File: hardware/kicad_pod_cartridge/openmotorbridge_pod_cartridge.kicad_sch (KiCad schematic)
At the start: 0 parts

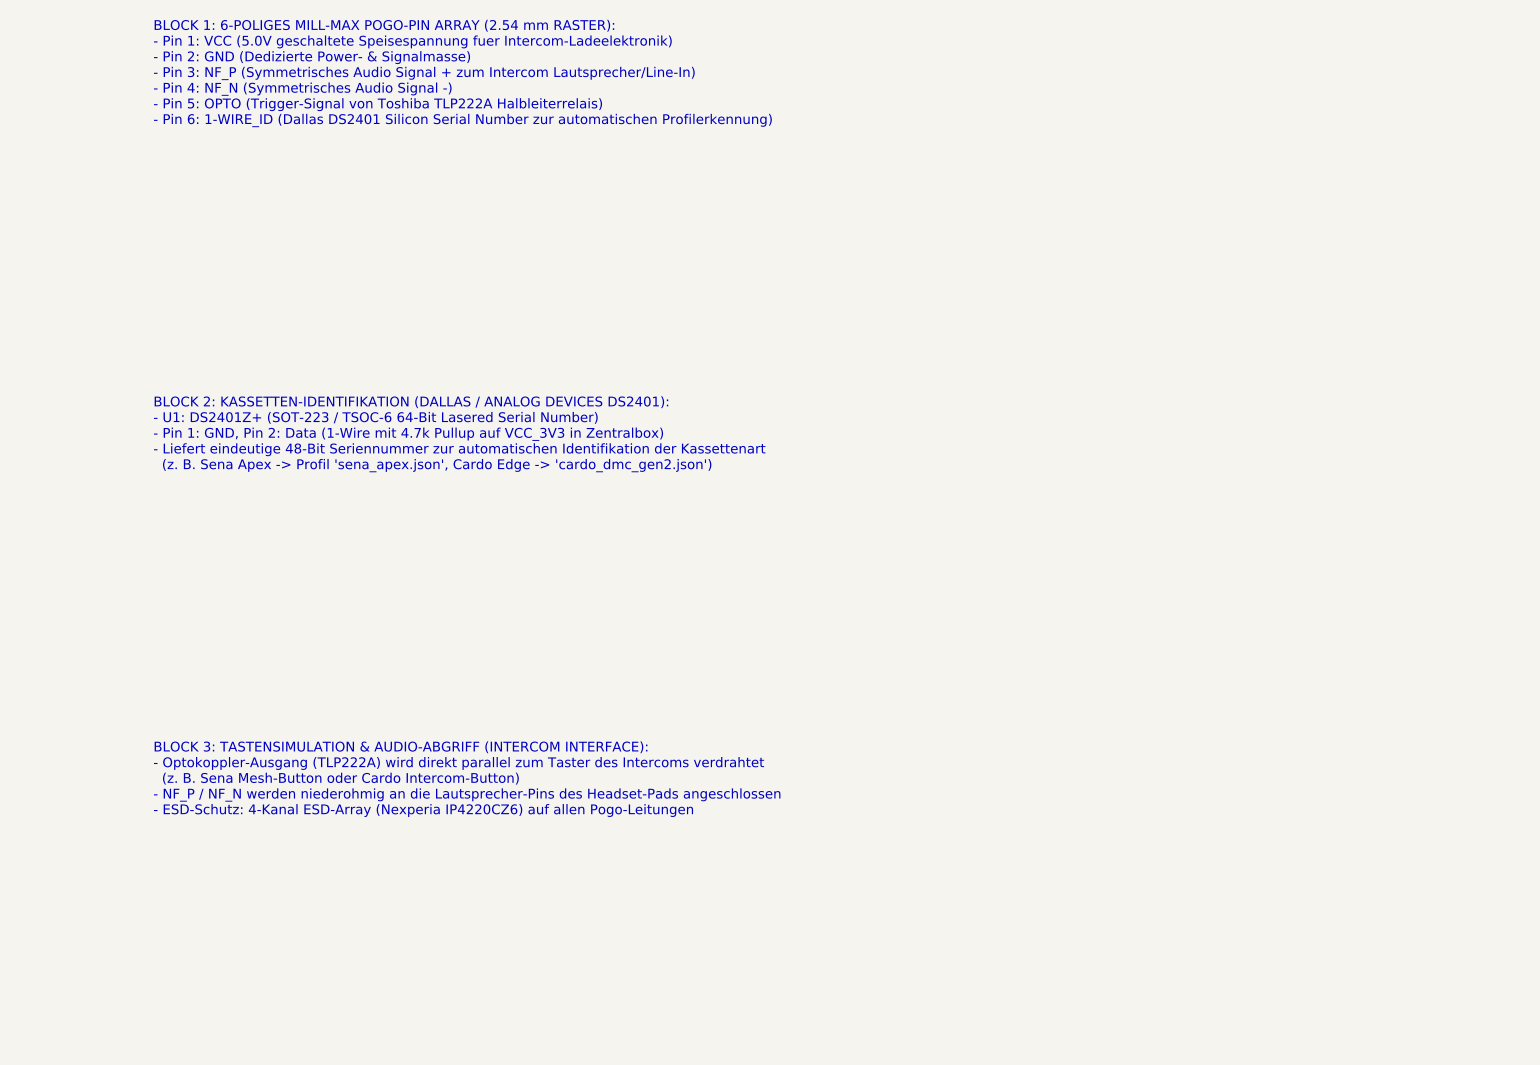
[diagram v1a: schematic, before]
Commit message: fix(kicad): Finalize KiCad 10 Pod 3 Transceiver and Universal Cartridge schematics and verified PDF exports
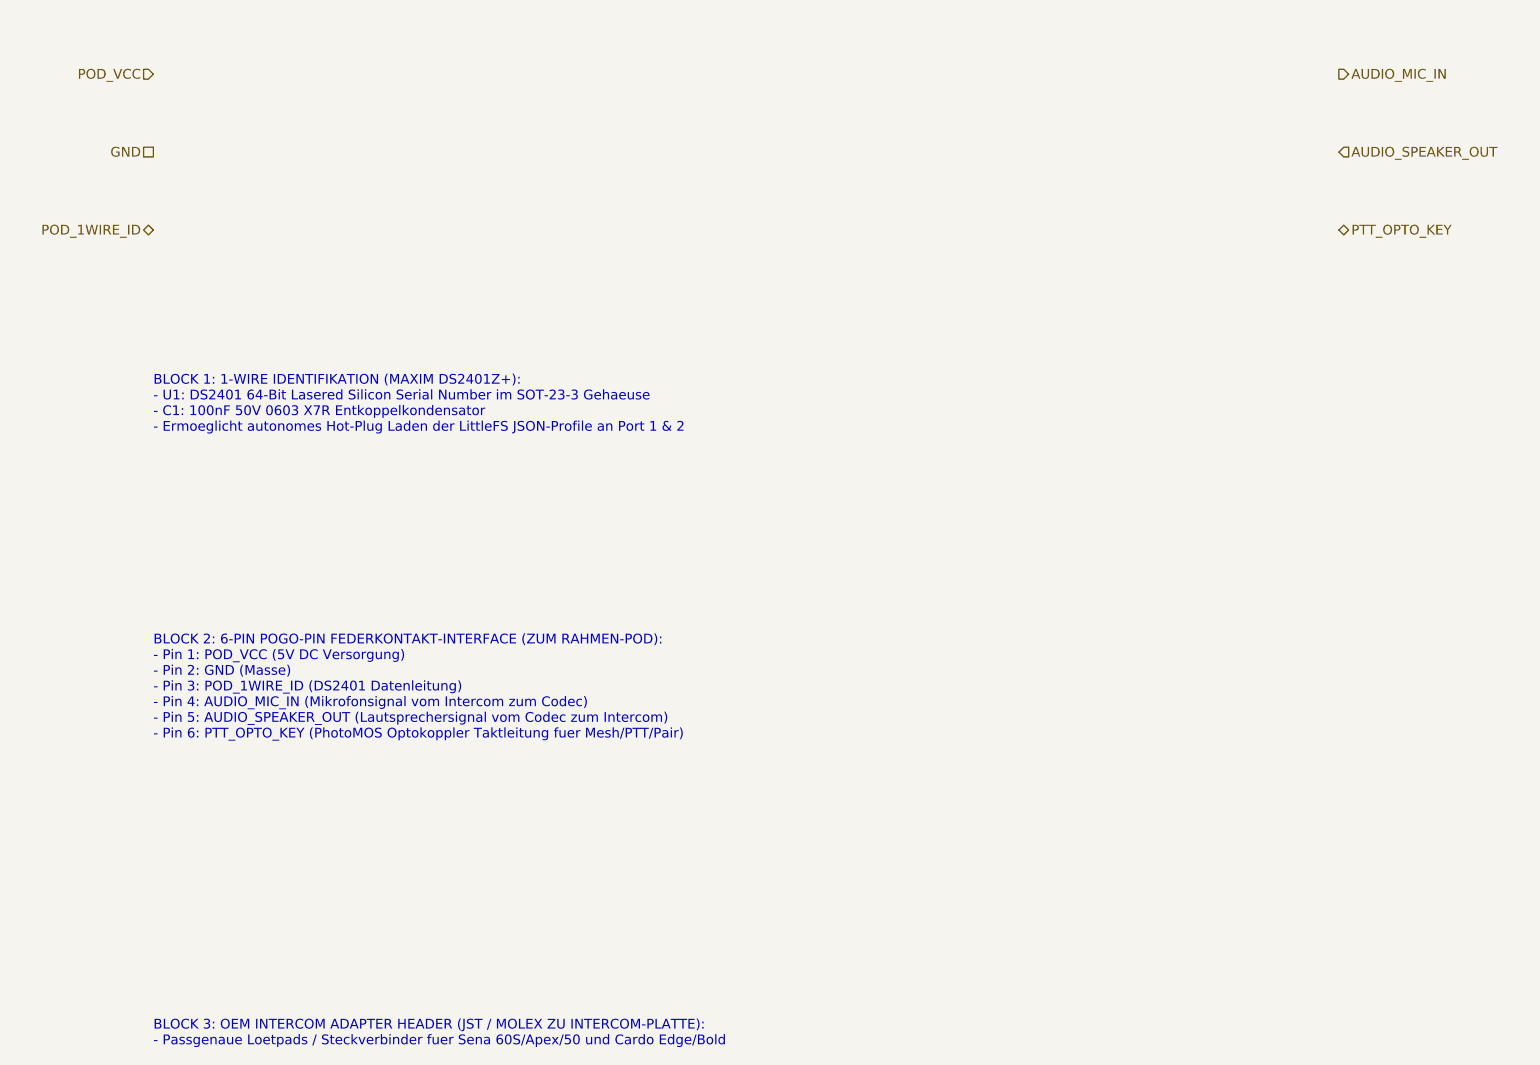
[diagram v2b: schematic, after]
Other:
- note added: "BLOCK 1: 1-WIRE IDENTIFIKATION (MAXIM DS2401Z+): - U1: DS2401 64-Bit Lasered Silicon Serial Number im SOT-23-3 Gehaeuse - C1: 100nF 50V 0603 X7R Entkoppelkondensator - Ermoeglicht autonomes Hot-Plug Laden der LittleFS JSON-Profile an Port 1 & 2"
- note added: "BLOCK 2: 6-PIN POGO-PIN FEDERKONTAKT-INTERFACE (ZUM RAHMEN-POD): - Pin 1: POD_VCC (5V DC Versorgung) - Pin 2: GND (Masse) - Pin 3: POD_1WIRE_ID (DS2401 Datenleitung) - Pin 4: AUDIO_MIC_IN (Mikrofonsignal vom Intercom zum Codec) - Pin 5: AUDIO_SPEAKER_OUT (Lautsprechersignal vom Codec zum Intercom) - Pin 6: PTT_OPTO_KEY (PhotoMOS Optokoppler Taktleitung fuer Mesh/PTT/Pair)"
- note added: "BLOCK 3: OEM INTERCOM ADAPTER HEADER (JST / MOLEX ZU INTERCOM-PLATTE): - Passgenaue Loetpads / Steckverbinder fuer Sena 60S/Apex/50 und Cardo Edge/Bold"
- note removed: "BLOCK 1: 6-POLIGES MILL-MAX POGO-PIN ARRAY (2.54 mm RASTER): - Pin 1: VCC (5.0V geschaltete Speisespannung fuer Intercom-Ladeelektronik) - Pin 2: GND (Dedizierte Power- & Signalmasse) - Pin 3: NF_P (Symmetrisches Audio Signal + zum Intercom Lautsprecher/Line-In) - Pin 4: NF_N (Symmetrisches Audio Signal -) - Pin 5: OPTO (Trigger-Signal von Toshiba TLP222A Halbleiterrelais) - Pin 6: 1-WIRE_ID (Dal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"
- note removed: "BLOCK 2: KASSETTEN-IDENTIFIKATION (DALLAS / ANALOG DEVICES DS2401): - U1: DS2401Z+ (SOT-223 / TSOC-6 64-Bit Lasered Serial Number) - Pin 1: GND, Pin 2: Data (1-Wire mit 4.7k Pullup auf VCC_3V3 in Zentralbox) - Liefert eindeutige 48-Bit Seriennummer zur automatischen Identifikation der Kassettenart (z. B. Sena Apex -> Profil 'sena_apex.json', Cardo Edge -> 'cardo_dmc_gen2.json')"
- note removed: "BLOCK 3: TASTENSIMULATION & AUDIO-ABGRIFF (INTERCOM INTERFACE): - Optokoppler-Ausgang (TLP222A) wird direkt parallel zum Taster des Intercoms verdrahtet (z. B. Sena Mesh-Button oder Cardo Intercom-Button) - NF_P / NF_N werden niederohmig an die Lautsprecher-Pins des Headset-Pads angeschlossen - ESD-Schutz: 4-Kanal ESD-Array (Nexperia IP4220CZ6) auf allen Pogo-Leitungen"
- title: OpenMotorBridge v8.0 - Universelle Kassetten-Platine (Pod 1 & Pod 2) -> OpenMotorBridge v8.0 - Universal Pod Cartridge
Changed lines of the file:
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@@
   (paper "A4")
   (title_block
-    (title "OpenMotorBridge v8.0 - Universelle Kassetten-Platine (Pod 1 & Pod 2)")
-    (date "2026-08-23")
+    (title "OpenMotorBridge v8.0 - Universal Pod Cartridge")
+    (date "2026-08-24")
     (rev "v8.0")
     (company "OpenMotorBridge Open Source Hardware")
-    (comment 1 "Mill-Max 6-Pin Pogo-Array (Serie 824-22-006-00-001101)")
-    (comment 2 "Maxim DS2401 1-Wire Silicon Serial Number + Opto-Trigger + Audio Interface")
+    (comment 1 "DS2401 Silicon Serial ROM ID + 6-Pin Pogo-Pin Matrix Interface")
+    (comment 2 "Kassettenträgerplatine für Sena, Cardo, PMR446 & Custom Inlays")
   )
-  (text "BLOCK 1: 6-POLIGES MILL-MAX POGO-PIN ARRAY (2.54 mm RASTER):\n- Pin 1: VCC (5.0V geschaltete Speisespannung fuer Intercom-Ladeelektronik)\n- Pin 2: GND (Dedizierte Power- & Signalmasse)\n- Pin 3: NF_P (Symmetrisches Audio Signal + zum Intercom Lautsprecher/Line-In)\n- Pin 4: NF_N (Symmetrisches Audio Signal -)\n- Pin 5: OPTO (Trigger-Signal von Toshiba TLP222A Halbleiterrelais)\n- Pin 6: 1-WIRE_ID (Dallas DS2401 Silicon Serial Number zur automatischen Profilerkennung)" (at 25.4 45.0 0)
+  (hierarchical_label "POD_VCC" (shape input) (at 25.4 38.1 180)
+    (effects (font (size 1.27 1.27)) (justify right))
+  )
+  (hierarchical_label "GND" (shape passive) (at 25.4 48.26 180)
+    (effects (font (size 1.27 1.27)) (justify right))
+  )
+  (hierarchical_label "POD_1WIRE_ID" (shape bidirectional) (at 25.4 58.42 180)
+    (effects (font (size 1.27 1.27)) (justify right))
+  )
+  (hierarchical_label "AUDIO_MIC_IN" (shape output) (at 180.0 38.1 0)
+    (effects (font (size 1.27 1.27)) (justify left))
+  )
+  (hierarchical_label "AUDIO_SPEAKER_OUT" (shape input) (at 180.0 48.26 0)
+    (effects (font (size 1.27 1.27)) (justify left))
+  )
+  (hierarchical_label "PTT_OPTO_KEY" (shape bidirectional) (at 180.0 58.42 0)
+    (effects (font (size 1.27 1.27)) (justify left))
+  )
+  (text "BLOCK 1: 1-WIRE IDENTIFIKATION (MAXIM DS2401Z+):\n- U1: DS2401 64-Bit Lasered Silicon Serial Number im SOT-23-3 Gehaeuse\n- C1: 100nF 50V 0603 X7R Entkoppelkondensator\n- Ermoeglicht autonomes Hot-Plug Laden der LittleFS JSON-Profile an Port 1 & 2" (at 25.4 85.0 0)
     (effects (font (size 1.27 1.27)) (justify left bottom))
   )
-  (text "BLOCK 2: KASSETTEN-IDENTIFIKATION (DALLAS / ANALOG DEVICES DS2401):\n- U1: DS2401Z+ (SOT-223 / TSOC-6 64-Bit Lasered Serial Number)\n- Pin 1: GND, Pin 2: Data (1-Wire mit 4.7k Pullup auf VCC_3V3 in Zentralbox)\n- Liefert eindeutige 48-Bit Seriennummer zur automatischen Identifikation der Kassettenart\n  (z. B. Sena Apex -> Profil 'sena_apex.json', Cardo Edge -> 'cardo_dmc_gen2.json')" (at 25.4 90.0 0)
+  (text "BLOCK 2: 6-PIN POGO-PIN FEDERKONTAKT-INTERFACE (ZUM RAHMEN-POD):\n- Pin 1: POD_VCC (5V DC Versorgung)\n- Pin 2: GND (Masse)\n- Pin 3: POD_1WIRE_ID (DS2401 Datenleitung)\n- Pin 4: AUDIO_MIC_IN (Mikrofonsignal vom Intercom zum Codec)\n- Pin 5: AUDIO_SPEAKER_OUT (Lautsprechersignal vom Codec zum Intercom)\n- Pin 6: PTT_OPTO_KEY (PhotoMOS Optokoppler Taktleitung fuer Mesh/PTT/Pair)" (at 25.4 125.0 0)
     (effects (font (size 1.27 1.27)) (justify left bottom))
   )
-  (text "BLOCK 3: TASTENSIMULATION & AUDIO-ABGRIFF (INTERCOM INTERFACE):\n- Optokoppler-Ausgang (TLP222A) wird direkt parallel zum Taster des Intercoms verdrahtet\n  (z. B. Sena Mesh-Button oder Cardo Intercom-Button)\n- NF_P / NF_N werden niederohmig an die Lautsprecher-Pins des Headset-Pads angeschlossen\n- ESD-Schutz: 4-Kanal ESD-Array (Nexperia IP4220CZ6) auf allen Pogo-Leitungen" (at 25.4 135.0 0)
+  (text "BLOCK 3: OEM INTERCOM ADAPTER HEADER (JST / MOLEX ZU INTERCOM-PLATTE):\n- Passgenaue Loetpads / Steckverbinder fuer Sena 60S/Apex/50 und Cardo Edge/Bold" (at 25.4 165.0 0)
     (effects (font (size 1.27 1.27)) (justify left bottom))
   )

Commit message: feat(kicad): Implement full graphical electronic schematic drawings (symbols, pins, wires, components) for all boards
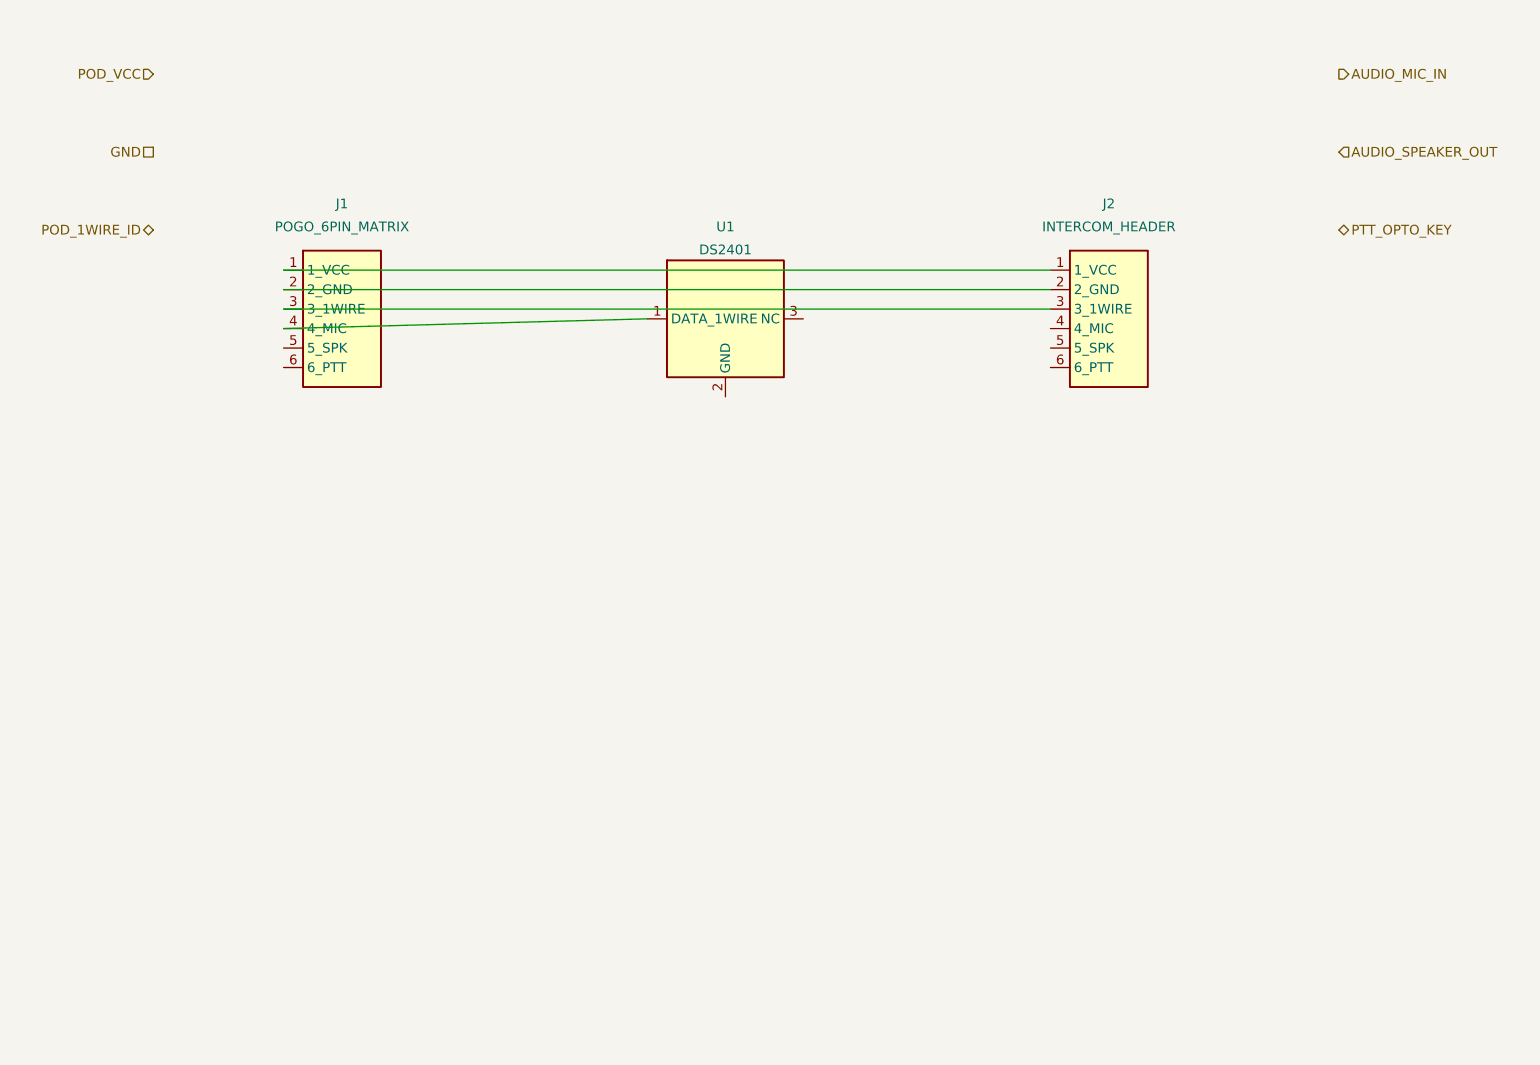
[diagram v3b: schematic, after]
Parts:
- added J1: POGO_6PIN_MATRIX, symbol Connector:Conn_01x06
- added J2: INTERCOM_HEADER, symbol Connector:Conn_01x06
- added U1: DS2401, symbol Memory_EEPROM:DS2401P
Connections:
- new net: J1.1 (1_VCC), J2.1 (1_VCC)
- new net: J1.2 (2_GND), J2.2 (2_GND)
- new net: J1.3 (3_1WIRE), J2.3 (3_1WIRE)
- new net: J1.4 (4_MIC), U1.1 (DATA_1WIRE)
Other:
- note removed: "BLOCK 1: 1-WIRE IDENTIFIKATION (MAXIM DS2401Z+): - U1: DS2401 64-Bit Lasered Silicon Serial Number im SOT-23-3 Gehaeuse - C1: 100nF 50V 0603 X7R Entkoppelkondensator - Ermoeglicht autonomes Hot-Plug Laden der LittleFS JSON-Profile an Port 1 & 2"
- note removed: "BLOCK 2: 6-PIN POGO-PIN FEDERKONTAKT-INTERFACE (ZUM RAHMEN-POD): - Pin 1: POD_VCC (5V DC Versorgung) - Pin 2: GND (Masse) - Pin 3: POD_1WIRE_ID (DS2401 Datenleitung) - Pin 4: AUDIO_MIC_IN (Mikrofonsignal vom Intercom zum Codec) - Pin 5: AUDIO_SPEAKER_OUT (Lautsprechersignal vom Codec zum Intercom) - Pin 6: PTT_OPTO_KEY (PhotoMOS Optokoppler Taktleitung fuer Mesh/PTT/Pair)"
- note removed: "BLOCK 3: OEM INTERCOM ADAPTER HEADER (JST / MOLEX ZU INTERCOM-PLATTE): - Passgenaue Loetpads / Steckverbinder fuer Sena 60S/Apex/50 und Cardo Edge/Bold"
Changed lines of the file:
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@@
-(kicad_sch (version 20260206) (generator "eeschema") (generator_version "10.0")
-  (paper "A4")
-  (title_block
-    (title "OpenMotorBridge v8.0 - Universal Pod Cartridge")
-    (date "2026-08-24")
-    (rev "v8.0")
-    (company "OpenMotorBridge Open Source Hardware")
-    (comment 1 "DS2401 Silicon Serial ROM ID + 6-Pin Pogo-Pin Matrix Interface")
-    (comment 2 "Kassettenträgerplatine für Sena, Cardo, PMR446 & Custom Inlays")
-  )
-  (hierarchical_label "POD_VCC" (shape input) (at 25.4 38.1 180)
-    (effects (font (size 1.27 1.27)) (justify right))
-  )
-  (hierarchical_label "GND" (shape passive) (at 25.4 48.26 180)
-    (effects (font (size 1.27 1.27)) (justify right))
-  )
-  (hierarchical_label "POD_1WIRE_ID" (shape bidirectional) (at 25.4 58.42 180)
-    (effects (font (size 1.27 1.27)) (justify right))
-  )
-  (hierarchical_label "AUDIO_MIC_IN" (shape output) (at 180.0 38.1 0)
-    (effects (font (size 1.27 1.27)) (justify left))
-  )
-  (hierarchical_label "AUDIO_SPEAKER_OUT" (shape input) (at 180.0 48.26 0)
-    (effects (font (size 1.27 1.27)) (justify left))
-  )
-  (hierarchical_label "PTT_OPTO_KEY" (shape bidirectional) (at 180.0 58.42 0)
-    (effects (font (size 1.27 1.27)) (justify left))
-  )
-  (text "BLOCK 1: 1-WIRE IDENTIFIKATION (MAXIM DS2401Z+):\n- U1: DS2401 64-Bit Lasered Silicon Serial Number im SOT-23-3 Gehaeuse\n- C1: 100nF 50V 0603 X7R Entkoppelkondensator\n- Ermoeglicht autonomes Hot-Plug Laden der LittleFS JSON-Profile an Port 1 & 2" (at 25.4 85.0 0)
-    (effects (font (size 1.27 1.27)) (justify left bottom))
-  )
-  (text "BLOCK 2: 6-PIN POGO-PIN FEDERKONTAKT-INTERFACE (ZUM RAHMEN-POD):\n- Pin 1: POD_VCC (5V DC Versorgung)\n- Pin 2: GND (Masse)\n- Pin 3: POD_1WIRE_ID (DS2401 Datenleitung)\n- Pin 4: AUDIO_MIC_IN (Mikrofonsignal vom Intercom zum Codec)\n- Pin 5: AUDIO_SPEAKER_OUT (Lautsprechersignal vom Codec zum Intercom)\n- Pin 6: PTT_OPTO_KEY (PhotoMOS Optokoppler Taktleitung fuer Mesh/PTT/Pair)" (at 25.4 125.0 0)
-    (effects (font (size 1.27 1.27)) (justify left bottom))
-  )
-  (text "BLOCK 3: OEM INTERCOM ADAPTER HEADER (JST / MOLEX ZU INTERCOM-PLATTE):\n- Passgenaue Loetpads / Steckverbinder fuer Sena 60S/Apex/50 und Cardo Edge/Bold" (at 25.4 165.0 0)
-    (effects (font (size 1.27 1.27)) (justify left bottom))
-  )
+(kicad_sch
+	(version 20260206)
+	(generator "eeschema")
+	(generator_version "10.0")
+	(paper "A4")
+	(title_block
+		(title "OpenMotorBridge v8.0 - Universal Pod Cartridge")
+		(date "2026-08-24")
+		(rev "v8.0")
+		(company "OpenMotorBridge Open Source Hardware")
+		(comment 1 "DS2401 Silicon Serial ROM ID + 6-Pin Pogo-Pin Matrix Interface")
+		(comment 2 "Kassettenträgerplatine für Sena, Cardo, PMR446 & Custom Inlays")
+	)
+	;; =========================================================================
+	;; Hierarchical Labels
+	;; =========================================================================
+	(hierarchical_label "POD_VCC" (shape input) (at 25.4 38.1 180) (effects (font (size 1.27 1.27)) (justify right)))
+	(hierarchical_label "GND" (shape passive) (at 25.4 48.26 180) (effects (font (size 1.27 1.27)) (justify right)))
+	(hierarchical_label "POD_1WIRE_ID" (shape bidirectional) (at 25.4 58.42 180) (effects (font (size 1.27 1.27)) (justify right)))
+	(hierarchical_label "AUDIO_MIC_IN" (shape output) (at 180.0 38.1 0) (effects (font (size 1.27 1.27)) (justify left)))
+	(hierarchical_label "AUDIO_SPEAKER_OUT" (shape input) (at 180.0 48.26 0) (effects (font (size 1.27 1.27)) (justify left)))
+	(hierarchical_label "PTT_OPTO_KEY" (shape bidirectional) (at 180.0 58.42 0) (effects (font (size 1.27 1.27)) (justify left)))
+	;; =========================================================================
+	;; Symbols Placement
+	;; =========================================================================
+	;; J1: 6-Pin Pogo Contact Interface
+	(symbol (lib_id "Connector:Conn_01x06") (at 50.0 70.0 0) (unit 1)
+		(in_bom yes) (on_board yes) (dnp no)
+		(property "Reference" "J1" (at 50.0 55.0 0) (effects (font (size 1.27 1.27))))
+		(property "Value" "POGO_6PIN_MATRIX" (at 50.0 58.0 0) (effects (font (size 1.27 1.27))))
+		(pin "1")
+		(pin "2")
+		(pin "3")
+		(pin "4")
+		(pin "5")
+		(pin "6")
+	)
+	;; U1: DS2401 Silicon Serial ROM
+	(symbol (lib_id "Memory_EEPROM:DS2401P") (at 100.0 70.0 0) (unit 1)
+		(in_bom yes) (on_board yes) (dnp no)
+		(property "Reference" "U1" (at 100.0 58.0 0) (effects (font (size 1.27 1.27))))
+		(property "Value" "DS2401" (at 100.0 61.0 0) (effects (font (size 1.27 1.27))))
+		(pin "1")
+		(pin "2")
+		(pin "3")
+	)
+	;; J2: Intercom Adapter Header
+	(symbol (lib_id "Connector:Conn_01x06") (at 150.0 70.0 0) (unit 1)
+		(in_bom yes) (on_board yes) (dnp no)
+		(property "Reference" "J2" (at 150.0 55.0 0) (effects (font (size 1.27 1.27))))
+		(property "Value" "INTERCOM_HEADER" (at 150.0 58.0 0) (effects (font (size 1.27 1.27))))
+		(pin "1")
+		(pin "2")
+		(pin "3")
+		(pin "4")
+		(pin "5")
+		(pin "6")
+	)
+	;; Wires
+	(wire (pts (xy 42.38 71.27) (xy 89.84 70.0)) (stroke (width 0) (type solid)))
+	(wire (pts (xy 42.38 68.73) (xy 142.38 68.73)) (stroke (width 0) (type solid)))
+	(wire (pts (xy 42.38 66.19) (xy 142.38 66.19)) (stroke (width 0) (type solid)))
+	(wire (pts (xy 42.38 63.65) (xy 142.38 63.65)) (stroke (width 0) (type solid)))
 )
